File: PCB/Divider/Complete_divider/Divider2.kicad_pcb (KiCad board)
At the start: 2 copper layers, 103.8 x 48 mm, 52 parts

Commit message: Reorganize
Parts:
- removed E30: Electr., Connector:Pad_for_electrode
- removed the R43 at (101.1, 87.7)
- added E43: Electr., Connector:Pad_for_electrode, F.Cu at (142.8, 109.3)
- added E56: Electr., Connector:Pad_for_electrode, F.Cu at (189.6, 74.3)
- added E57: Electr., Connector:Pad_for_electrode, F.Cu at (193.2, 109.2)
- added J31: Electr., Connector_Pin:Pin_D1.0mm_L10.0mm, F.Cu at (99.6, 100.6)
- added J58: Electr., Connector_Pin:Pin_D1.0mm_L10.0mm, F.Cu at (193.2, 81.8)
- added R58: 10M, Resistor_SMD:R_1206_3216Metric, F.Cu at (193.2, 95.7)
- moved E42 62.7 mm to (139.2, 74.3)
- moved E40 56.8 mm to (132.0, 74.3)
- moved E38 51.3 mm to (124.8, 74.3)
- moved E45 48.8 mm to (150.0, 109.3)
- moved E41 48.3 mm to (135.6, 109.3)
- moved E36 46.3 mm to (117.6, 74.3)
- moved E47 44.0 mm to (157.2, 109.3)
- moved E34 41.9 mm to (110.4, 74.3)
- moved E39 41.1 mm to (128.4, 109.3)
- moved E49 39.9 mm to (164.4, 109.3)
- moved E32 38.4 mm to (103.2, 74.3)
- moved E44 38.1 mm to (146.4, 74.3)
- moved E51 36.8 mm to (171.6, 109.3)
- moved E53 35.0 mm to (178.8, 109.3)
- moved E55 34.5 mm to (186.0, 109.3)
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- renumbered R30 to R32, R44 to R33, R31 to R34, R45 to R35, R32 to R36, R46 to R37, R33 to R38, R47 to R39, R34 to R40, R48 to R41, R35 to R42, R49 to R43, R36 to R44, R50 to R45, R37 to R46, R51 to R47, R38 to R48, R52 to R49, R39 to R50, R53 to R51, R40 to R52, R54 to R53, R41 to R54, R42 to R56, R56 to R57
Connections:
- E31 pad 1: Net-(E31-Pad1) -> DRIFTTUBE
- R32 pad 1: Net-(E30-Pad1) -> Net-(E32-Pad1)
- R32 pad 2: Net-(R30-Pad2) -> DRIFTTUBE
- R33 pad 1: Net-(E30-Pad1) -> Net-(E32-Pad1)
- R33 pad 2: Net-(E44-Pad1) -> Net-(E33-Pad1)
- R34 pad 1: Net-(E31-Pad1) -> Net-(E34-Pad1)
- R34 pad 2: Net-(E44-Pad1) -> Net-(E33-Pad1)
- R35 pad 1: Net-(E31-Pad1) -> Net-(E34-Pad1)
- R35 pad 2: Net-(E45-Pad1) -> Net-(E35-Pad1)
- R36 pad 1: Net-(E32-Pad1) -> Net-(E36-Pad1)
- R36 pad 2: Net-(E45-Pad1) -> Net-(E35-Pad1)
- R37 pad 1: Net-(E32-Pad1) -> Net-(E36-Pad1)
- R37 pad 2: Net-(E46-Pad1) -> Net-(E37-Pad1)
- R38 pad 1: Net-(E33-Pad1) -> Net-(E38-Pad1)
- R38 pad 2: Net-(E46-Pad1) -> Net-(E37-Pad1)
- R39 pad 1: Net-(E33-Pad1) -> Net-(E38-Pad1)
- R39 pad 2: Net-(E47-Pad1) -> Net-(E39-Pad1)
- R40 pad 1: Net-(E34-Pad1) -> Net-(E40-Pad1)
- R40 pad 2: Net-(E47-Pad1) -> Net-(E39-Pad1)
- R41 pad 1: Net-(E34-Pad1) -> Net-(E40-Pad1)
- R41 pad 2: Net-(E48-Pad1) -> Net-(E41-Pad1)
- R42 pad 1: Net-(E35-Pad1) -> Net-(E42-Pad1)
- R42 pad 2: Net-(E48-Pad1) -> Net-(E41-Pad1)
- R43 pad 1: Net-(E35-Pad1) -> Net-(E42-Pad1)
- R43 pad 2: Net-(E49-Pad1) -> Net-(E43-Pad1)
- R44 pad 1: Net-(E36-Pad1) -> Net-(E44-Pad1)
- R44 pad 2: Net-(E49-Pad1) -> Net-(E43-Pad1)
- R45 pad 1: Net-(E36-Pad1) -> Net-(E44-Pad1)
- R45 pad 2: Net-(E50-Pad1) -> Net-(E45-Pad1)
- R46 pad 1: Net-(E37-Pad1) -> Net-(E46-Pad1)
- R46 pad 2: Net-(E50-Pad1) -> Net-(E45-Pad1)
- R47 pad 1: Net-(E37-Pad1) -> Net-(E46-Pad1)
- R47 pad 2: Net-(E51-Pad1) -> Net-(E47-Pad1)
- R48 pad 1: Net-(E38-Pad1) -> Net-(E48-Pad1)
- R48 pad 2: Net-(E51-Pad1) -> Net-(E47-Pad1)
- R49 pad 1: Net-(E38-Pad1) -> Net-(E48-Pad1)
- R49 pad 2: Net-(E52-Pad1) -> Net-(E49-Pad1)
- R50 pad 1: Net-(E39-Pad1) -> Net-(E50-Pad1)
- R50 pad 2: Net-(E52-Pad1) -> Net-(E49-Pad1)
- R51 pad 1: Net-(E39-Pad1) -> Net-(E50-Pad1)
- R51 pad 2: Net-(E53-Pad1) -> Net-(E51-Pad1)
- R52 pad 1: Net-(E40-Pad1) -> Net-(E52-Pad1)
- R52 pad 2: Net-(E53-Pad1) -> Net-(E51-Pad1)
- R53 pad 1: Net-(E40-Pad1) -> Net-(E52-Pad1)
- R53 pad 2: Net-(E54-Pad1) -> Net-(E53-Pad1)
- R54 pad 1: Net-(E41-Pad1) -> Net-(E54-Pad1)
- R54 pad 2: Net-(E54-Pad1) -> Net-(E53-Pad1)
- R55 pad 1: Net-(E41-Pad1) -> Net-(E54-Pad1)
- R56 pad 1: Net-(E42-Pad1) -> Net-(E56-Pad1)
- R57 pad 1: Net-(E42-Pad1) -> Net-(E56-Pad1)
- R57 pad 2: APGRID -> Net-(E57-Pad1)
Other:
- board size 103.8 x 48 mm -> 98 x 48 mm

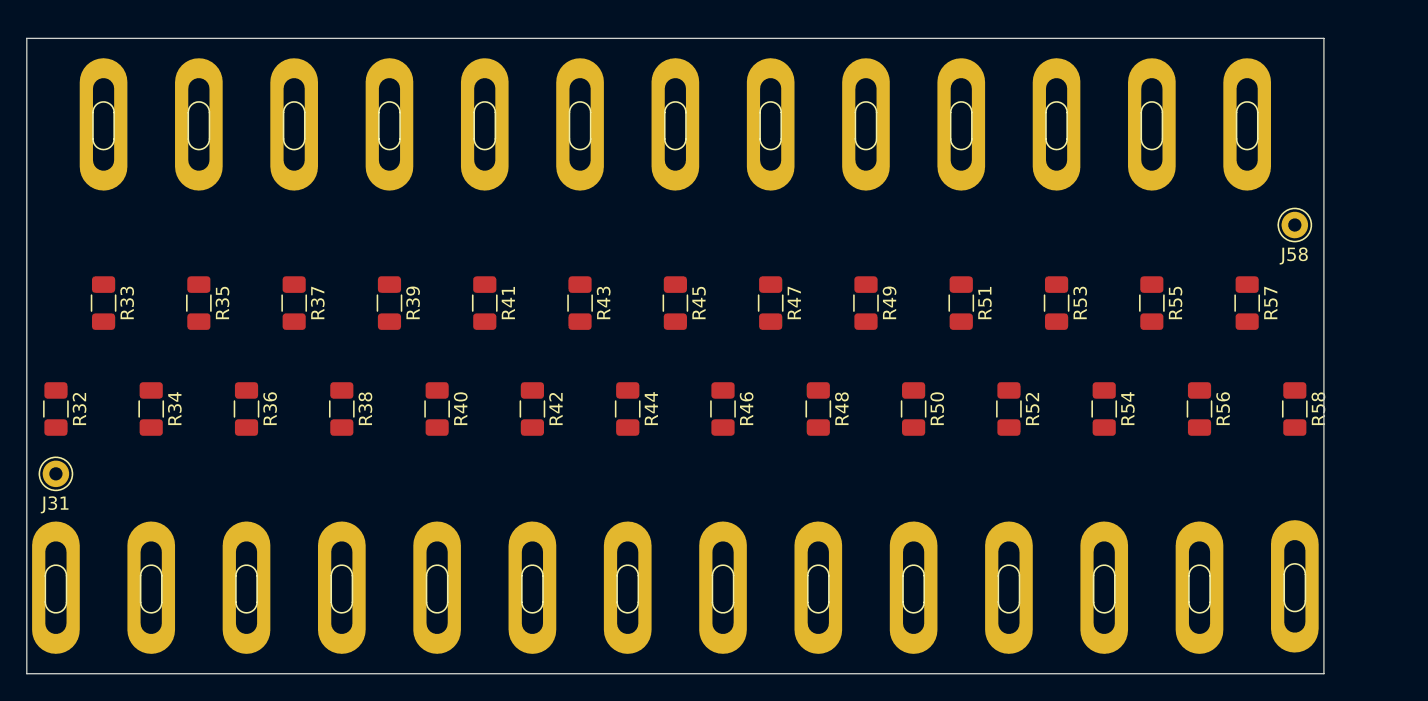
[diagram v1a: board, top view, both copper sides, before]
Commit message: Dividers finished without testing points
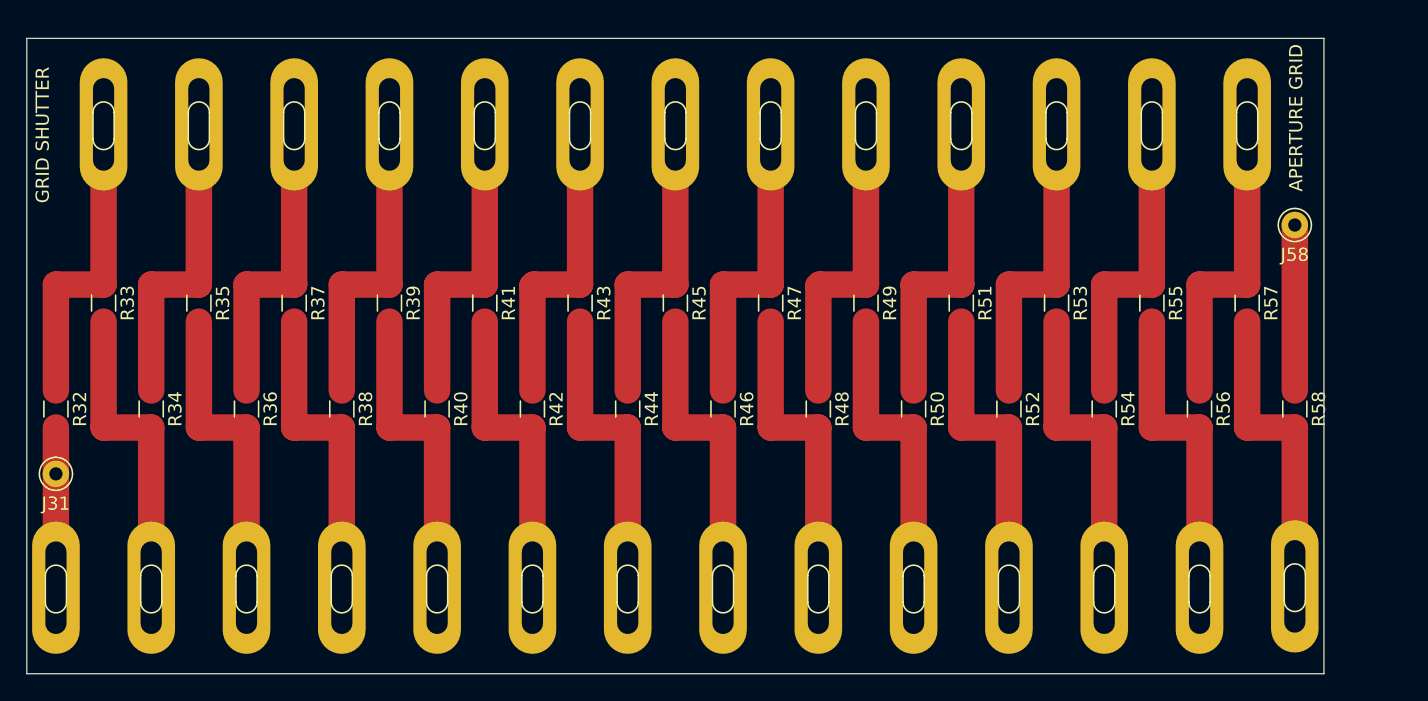
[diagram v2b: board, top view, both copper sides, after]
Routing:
- net Net-(E53-Pad1): track 0.00 -> 23.7 mm
- net Net-(E43-Pad1): track 0.00 -> 23.7 mm
- net Net-(E39-Pad1): track 0.00 -> 23.7 mm
- net Net-(E37-Pad1): track 0.00 -> 23.7 mm
- net Net-(E55-Pad1): track 0.00 -> 23.7 mm
- net Net-(E51-Pad1): track 0.00 -> 23.7 mm
- net Net-(E49-Pad1): track 0.00 -> 23.7 mm
- net Net-(E47-Pad1): track 0.00 -> 23.7 mm
- net Net-(E45-Pad1): track 0.00 -> 23.7 mm
- net Net-(E41-Pad1): track 0.00 -> 23.7 mm
- net Net-(E35-Pad1): track 0.00 -> 23.7 mm
- net Net-(E34-Pad1): track 0.00 -> 23.7 mm
- net Net-(E33-Pad1): track 0.00 -> 23.7 mm
- net Net-(E32-Pad1): track 0.00 -> 23.7 mm
- net Net-(E56-Pad1): track 0.00 -> 23.7 mm
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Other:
- board text added: "APERTURE GRID"
- board text added: "GRID SHUTTER"
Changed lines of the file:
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@@
   (general
     (thickness 1.6)
-    (drawings 14)
-    (tracks 0)
+    (drawings 16)
+    (tracks 83)
     (zones 0)
     (modules 56)
@@
     (38 B.Mask user)
     (39 F.Mask user)
-    (40 Dwgs.User user)
+    (40 Dwgs.User user hide)
     (41 Cmts.User user)
     (42 Eco1.User user)
@@
   )
   (setup
-    (last_trace_width 0.25)
+    (last_trace_width 2)
     (user_trace_width 2)
     (trace_clearance 0.2)
@@
     )
   )
+  (gr_text "APERTURE GRID\n" (at 193.3 73.7 90) (layer F.SilkS)
+    (effects (font (size 1 1) (thickness 0.15)))
+  )
+  (gr_text "GRID SHUTTER\n" (at 98.6 75 90) (layer F.SilkS)
+    (effects (font (size 1 1) (thickness 0.15)))
+  )
   (gr_line (start 98.3 95.7) (end 198.9 95.7) (layer Dwgs.User) (width 0.15))
   (gr_line (start 95.6 87.7) (end 196.2 87.7) (layer Dwgs.User) (width 0.15))
@@
     (arrow2b (pts (xy 29.434179 52.129268) (xy 30.035768 53.247745)))
   )
+  (segment (start 193.2 94.3) (end 193.2 81.8) (width 2) (layer F.Cu) (net 1))
+  (segment (start 99.6 109.2) (end 99.6 100.6) (width 2) (layer F.Cu) (net 2))
+  (segment (start 99.6 100.6) (end 99.6 97.1) (width 2) (layer F.Cu) (net 2))
+  (segment (start 103.2 74.2) (end 103.2 86.3) (width 2) (layer F.Cu) (net 3))
+  (segment (start 99.6 94.3) (end 99.6 86.3) (width 2) (layer F.Cu) (net 3))
+  (segment (start 99.6 86.3) (end 103.2 86.3) (width 2) (layer F.Cu) (net 3))
+  (segment (start 103.2 89.1) (end 103.2 97.1) (width 2) (layer F.Cu) (net 4))
+  (segment (start 103.2 97.1) (end 106.8 97.1) (width 2) (layer F.Cu) (net 4))
+  (segment (start 106.8 97.1) (end 106.8 109.2) (width 2) (layer F.Cu) (net 4))
+  (segment (start 110.4 74.2) (end 110.4 86.3) (width 2) (layer F.Cu) (net 5))
+  (segment (start 106.8 94.3) (end 106.8 86.3) (width 2) (layer F.Cu) (net 5))
+  (segment (start 106.8 86.3) (end 110.4 86.3) (width 2) (layer F.Cu) (net 5))
+  (segment (start 110.4 89.1) (end 110.4 97.1) (width 2) (layer F.Cu) (net 6))
+  (segment (start 110.4 97.1) (end 114 97.1) (width 2) (layer F.Cu) (net 6))
+  (segment (start 114 97.1) (end 114 109.2) (width 2) (layer F.Cu) (net 6))
+  (segment (start 114 94.3) (end 114 86.3) (width 2) (layer F.Cu) (net 7))
+  (segment (start 114 86.3) (end 117.6 86.3) (width 2) (layer F.Cu) (net 7))
+  (segment (start 117.6 74.2) (end 117.6 86.3) (width 2) (layer F.Cu) (net 7))
+  (segment (start 117.6 89.1) (end 117.6 97.1) (width 2) (layer F.Cu) (net 8))
+  (segment (start 117.6 97.1) (end 121.2 97.1) (width 2) (layer F.Cu) (net 8))
+  (segment (start 121.2 97.1) (end 121.2 109.2) (width 2) (layer F.Cu) (net 8))
+  (segment (start 121.2 94.3) (end 121.2 86.3) (width 2) (layer F.Cu) (net 9))
+  (segment (start 121.2 86.3) (end 124.8 86.3) (width 2) (layer F.Cu) (net 9))
+  (segment (start 124.8 74.2) (end 124.8 86.3) (width 2) (layer F.Cu) (net 9))
+  (segment (start 124.8 89.1) (end 124.8 97.1) (width 2) (layer F.Cu) (net 10))
+  (segment (start 124.8 97.1) (end 128.4 97.1) (width 2) (layer F.Cu) (net 10))
+  (segment (start 128.4 97.1) (end 128.4 109.2) (width 2) (layer F.Cu) (net 10))
+  (segment (start 128.4 94.3) (end 128.4 86.3) (width 2) (layer F.Cu) (net 11))
+  (segment (start 128.4 86.3) (end 132 86.3) (width 2) (layer F.Cu) (net 11))
+  (segment (start 132 86.3) (end 132 74.2) (width 2) (layer F.Cu) (net 11))
+  (segment (start 132 89.1) (end 132 97.1) (width 2) (layer F.Cu) (net 12))
+  (segment (start 132 97.1) (end 135.6 97.1) (width 2) (layer F.Cu) (net 12))
+  (segment (start 135.6 97.1) (end 135.6 109.2) (width 2) (layer F.Cu) (net 12))
+  (segment (start 135.6 94.3) (end 135.6 86.4) (width 2) (layer F.Cu) (net 13))
+  (segment (start 135.7 86.3) (end 139.2 86.3) (width 2) (layer F.Cu) (net 13))
+  (segment (start 135.6 86.4) (end 135.7 86.3) (width 2) (layer F.Cu) (net 13))
+  (segment (start 139.2 86.3) (end 139.2 74.2) (width 2) (layer F.Cu) (net 13))
+  (segment (start 139.2 89.1) (end 139.2 97.1) (width 2) (layer F.Cu) (net 14))
+  (segment (start 139.2 97.1) (end 142.8 97.1) (width 2) (layer F.Cu) (net 14))
+  (segment (start 142.8 97.1) (end 142.8 109.2) (width 2) (layer F.Cu) (net 14))
+  (segment (start 142.8 94.3) (end 142.8 86.3) (width 2) (layer F.Cu) (net 15))
+  (segment (start 142.8 86.3) (end 146.4 86.3) (width 2) (layer F.Cu) (net 15))
+  (segment (start 146.4 86.3) (end 146.4 74.2) (width 2) (layer F.Cu) (net 15))
+  (segment (start 146.4 89.1) (end 146.4 97.1) (width 2) (layer F.Cu) (net 16))
+  (segment (start 146.4 97.1) (end 150 97.1) (width 2) (layer F.Cu) (net 16))
+  (segment (start 150 109.2) (end 150 97.1) (width 2) (layer F.Cu) (net 16))
+  (segment (start 150 94.3) (end 150 86.3) (width 2) (layer F.Cu) (net 17))
+  (segment (start 150 86.3) (end 153.6 86.3) (width 2) (layer F.Cu) (net 17))
+  (segment (start 153.6 86.3) (end 153.6 74.2) (width 2) (layer F.Cu) (net 17))
+  (segment (start 153.6 89.1) (end 153.6 97.1) (width 2) (layer F.Cu) (net 18))
+  (segment (start 153.6 97.1) (end 157.2 97.1) (width 2) (layer F.Cu) (net 18))
+  (segment (start 157.2 109.2) (end 157.2 97.1) (width 2) (layer F.Cu) (net 18))
+  (segment (start 160.8 86.3) (end 160.8 74.2) (width 2) (layer F.Cu) (net 19))
+  (segment (start 157.2 94.3) (end 157.2 86.4) (width 2) (layer F.Cu) (net 19))
+  (segment (start 157.3 86.3) (end 160.8 86.3) (width 2) (layer F.Cu) (net 19))
+  (segment (start 157.2 86.4) (end 157.3 86.3) (width 2) (layer F.Cu) (net 19))
+  (segment (start 160.8 89.1) (end 160.8 97.1) (width 2) (layer F.Cu) (net 20))
+  (segment (start 160.8 97.1) (end 164.4 97.1) (width 2) (layer F.Cu) (net 20))
+  (segment (start 164.4 109.2) (end 164.4 97.1) (width 2) (layer F.Cu) (net 20))
+  (segment (start 168 74.2) (end 168 86.3) (width 2) (layer F.Cu) (net 21))
+  (segment (start 164.4 94.3) (end 164.4 86.3) (width 2) (layer F.Cu) (net 21))
+  (segment (start 164.4 86.3) (end 168 86.3) (width 2) (layer F.Cu) (net 21))
+  (segment (start 168 89.1) (end 168 97.1) (width 2) (layer F.Cu) (net 22))
+  (segment (start 168 97.1) (end 171.6 97.1) (width 2) (layer F.Cu) (net 22))
+  (segment (start 171.6 97.1) (end 171.6 109.2) (width 2) (layer F.Cu) (net 22))
+  (segment (start 175.2 86.3) (end 175.2 74.2) (width 2) (layer F.Cu) (net 23))
+  (segment (start 171.6 94.3) (end 171.6 86.3) (width 2) (layer F.Cu) (net 23))
+  (segment (start 171.6 86.3) (end 175.2 86.3) (width 2) (layer F.Cu) (net 23))
+  (segment (start 175.2 89.1) (end 175.2 97.1) (width 2) (layer F.Cu) (net 24))
+  (segment (start 175.2 97.1) (end 178.8 97.1) (width 2) (layer F.Cu) (net 24))
+  (segment (start 178.8 97.1) (end 178.8 109.2) (width 2) (layer F.Cu) (net 24))
+  (segment (start 178.8 94.3) (end 178.8 86.3) (width 2) (layer F.Cu) (net 25))
+  (segment (start 178.8 86.3) (end 182.4 86.3) (width 2) (layer F.Cu) (net 25))
+  (segment (start 182.4 86.3) (end 182.4 74.2) (width 2) (layer F.Cu) (net 25))
+  (segment (start 182.4 89.1) (end 182.4 97.1) (width 2) (layer F.Cu) (net 26))
+  (segment (start 182.4 97.1) (end 186 97.1) (width 2) (layer F.Cu) (net 26))
+  (segment (start 186 97.1) (end 186 109.2) (width 2) (layer F.Cu) (net 26))
+  (segment (start 186 94.3) (end 186 86.3) (width 2) (layer F.Cu) (net 27))
+  (segment (start 186 86.3) (end 189.6 86.3) (width 2) (layer F.Cu) (net 27))
+  (segment (start 189.6 86.3) (end 189.6 74.2) (width 2) (layer F.Cu) (net 27))
+  (segment (start 189.6 89.1) (end 189.6 97.1) (width 2) (layer F.Cu) (net 28))
+  (segment (start 189.6 97.1) (end 193.2 97.1) (width 2) (layer F.Cu) (net 28))
+  (segment (start 193.2 97.1) (end 193.2 109.1) (width 2) (layer F.Cu) (net 28))
 )
